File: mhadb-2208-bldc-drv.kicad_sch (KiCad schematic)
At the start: 46 parts, among them J1 TC2030, J2 Conn_01x04_Pin, J3 Conn_01x04, J4 Conn_01x04_Pin, SW1 SW_Push, SW4 SW_Push, U1 HT753-1, U2 SN65HVD230, U3 STM32F103C8Tx, Y1 8M

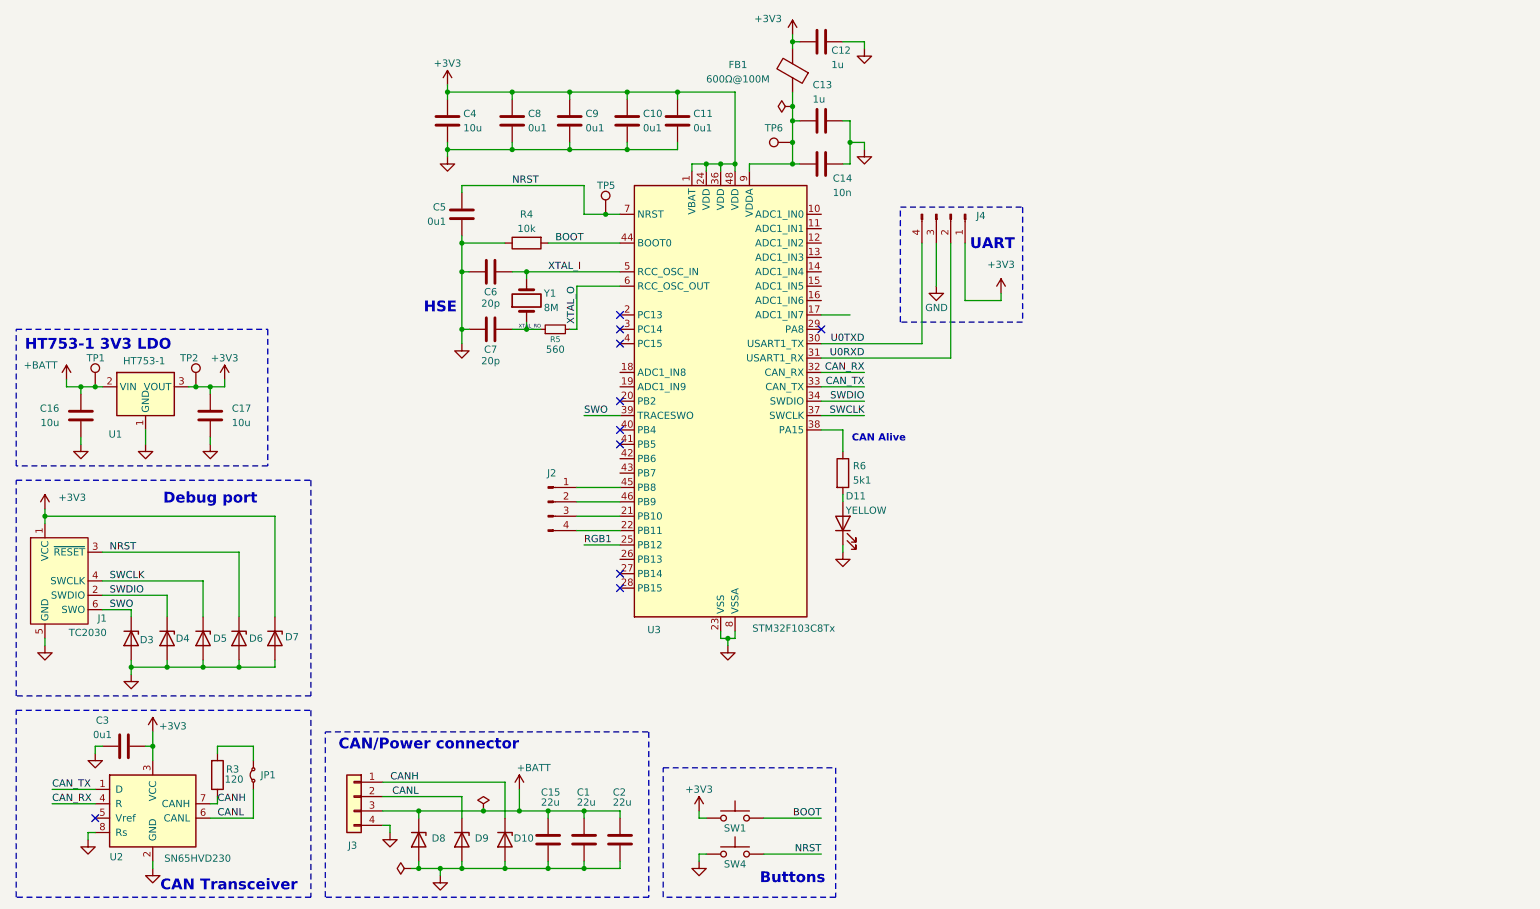
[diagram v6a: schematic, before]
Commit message: schem: add DRV8311 BLDC FOC driver
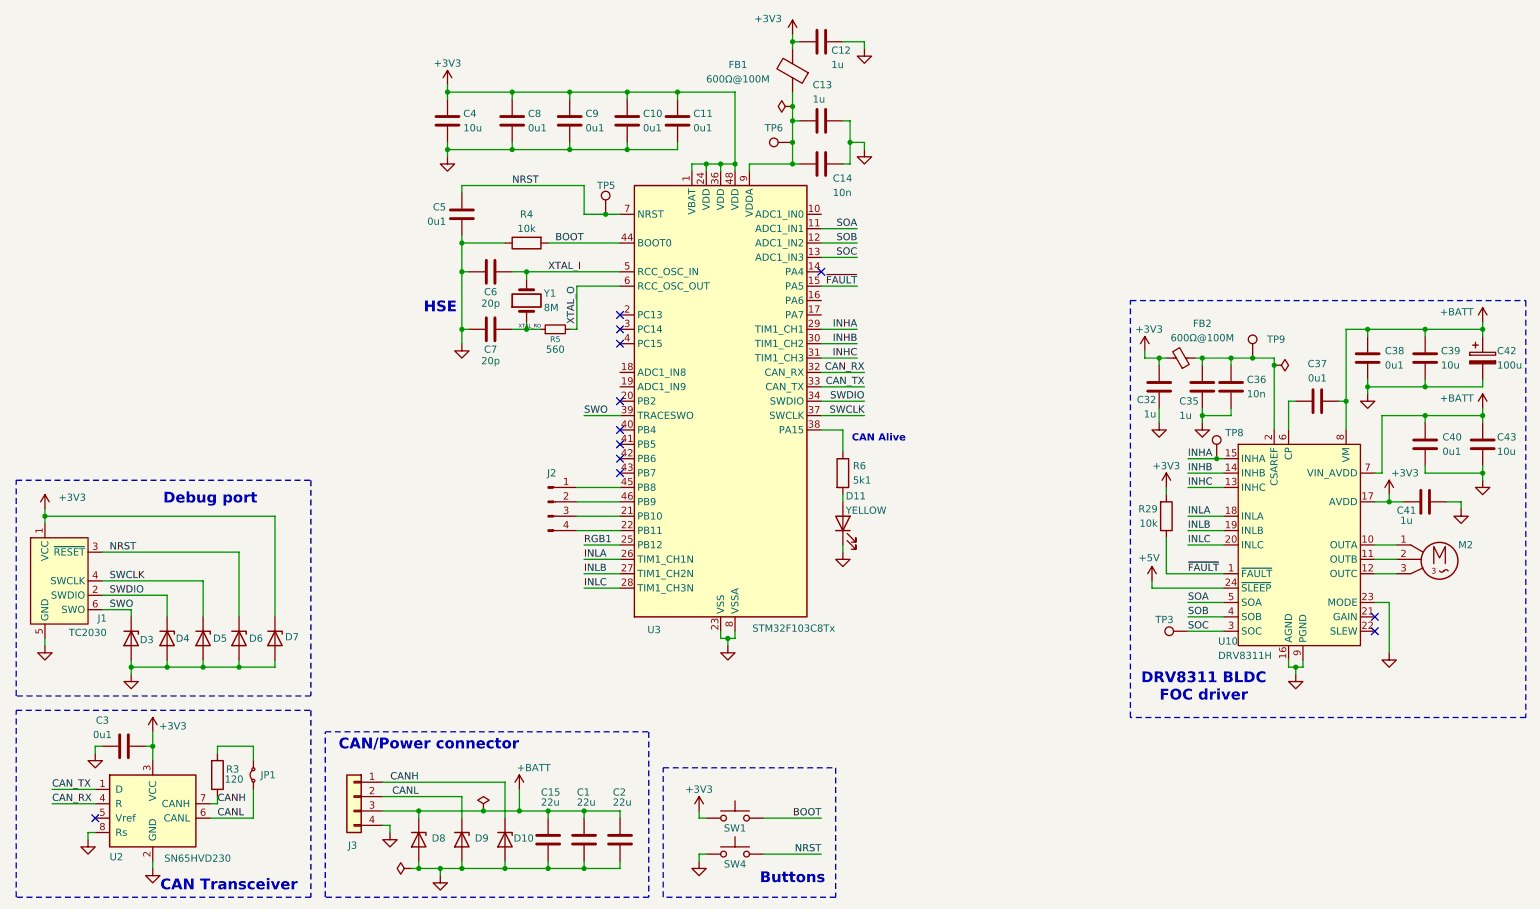
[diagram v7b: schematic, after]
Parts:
- removed C16, C17: 10u, Capacitor_SMD:C_0805_2012Metric, symbol Device:C
- removed J4: Conn_01x04_Pin, Connector_PinHeader_2.54mm:PinHeader_1x04_P2.54mm_Vertical, symbol Connector:Conn_01x04_Pin
- removed TP1, TP2: TestPoint, TestPoint:TestPoint_Pad_D2.0mm, symbol Connector:TestPoint
- removed U1: HT753-1, Package_TO_SOT_SMD:SOT-89-3, symbol Regulator_Linear:HT75xx-1-SOT89
- added C32, C35, C41: 1u, Capacitor_SMD:C_0402_1005Metric, symbol Device:C
- added C36: 10n, Capacitor_SMD:C_0402_1005Metric, symbol Device:C
- added C37, C38, C40: 0u1, Capacitor_SMD:C_0402_1005Metric, symbol Device:C
- added C39, C43: 10u, Capacitor_SMD:C_0805_2012Metric, symbol Device:C
- added C42: 100u, Capacitor_SMD:CP_Elec_6.3x7.7, symbol Device:C_Polarized
- added FB2: 600Ω@100M, Inductor_SMD:L_0805_2012Metric, symbol Device:FerriteBead_Small
- added M2: Motor_3_Phases, Connector_PinHeader_2.54mm:PinHeader_1x03_P2.54mm_Vertical, symbol GLCS:Motor_3_Phases
- added R29: 10k, Resistor_SMD:R_0402_1005Metric, symbol Device:R
- added TP3, TP8, TP9: TestPoint, TestPoint:TestPoint_Pad_D2.0mm, symbol Connector:TestPoint
- added U10: DRV8311H, GLCS:Texas_RRW0024A_WQFN-24-1EP_2x2mm_P0.4mmThermalVias, symbol GLCS:DRV8311H
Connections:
- net +3V3: now also C32.1, C41.1, FB2.2, R29.2, U10.17 (AVDD)
- net +BATT: now also C37.2, C38.2, C39.2, C40.2, C42.1, C43.2, U10.7 (VIN_AVDD), U10.8 (VM)
- net SOA: now reaches U3.11 (PA1)
- net SOA: now also U10.5 (SOA)
- net SOB: now reaches U3.12 (PA2)
- net SOB: now also U10.4 (SOB)
- net SOC: now reaches U3.13 (PA3)
- net SOC: now also TP3.1, U10.3 (SOC)
- net ~{FAULT}: now reaches U3.15 (PA5)
- net ~{FAULT}: now also R29.1, U10.1 (~{FAULT})
- net INLA: now reaches U3.26 (PB13)
- net INLA: now also U10.18 (INLA)
- net INLB: now reaches U3.27 (PB14)
- net INLB: now also U10.19 (INLB)
- net INLC: now reaches U3.28 (PB15)
- net INLC: now also U10.20 (INLC)
- net INHA: now reaches U3.29 (PA8)
- net INHA: now also TP8.1, U10.15 (INHA)
- net GND renamed EPAD
- net EPAD: now also C32.2, C35.2, C36.2, C38.1, C39.1, C40.1, C41.2, C42.2, C43.1, U10.16 (AGND), U10.23 (MODE), U10.25 (EPAD), U10.9 (PGND)
- net U0RXD renamed INHC
- net INHC: now also U10.13 (INHC)
- net U0TXD renamed INHB
- net INHB: now also U10.14 (INHB)
- new net: C35.1, C36.1, FB2.1, TP9.1, U10.2 (CSAREF)
- new net: M2.1, U10.10 (OUTA)
- new net: M2.2, U10.11 (OUTB)
- new net: M2.3, U10.12 (OUTC)
- new net: C37.1, U10.6 (CP)
- new net +5V: U10.24 (~{SLEEP})
- no-connect marks 10 -> 12
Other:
- note added: "DRV8311 BLDC FOC driver"
- note removed: "HT753-1 3V3 LDO"
- note removed: "UART"

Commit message: schem: add AS5600 magnetic encoder
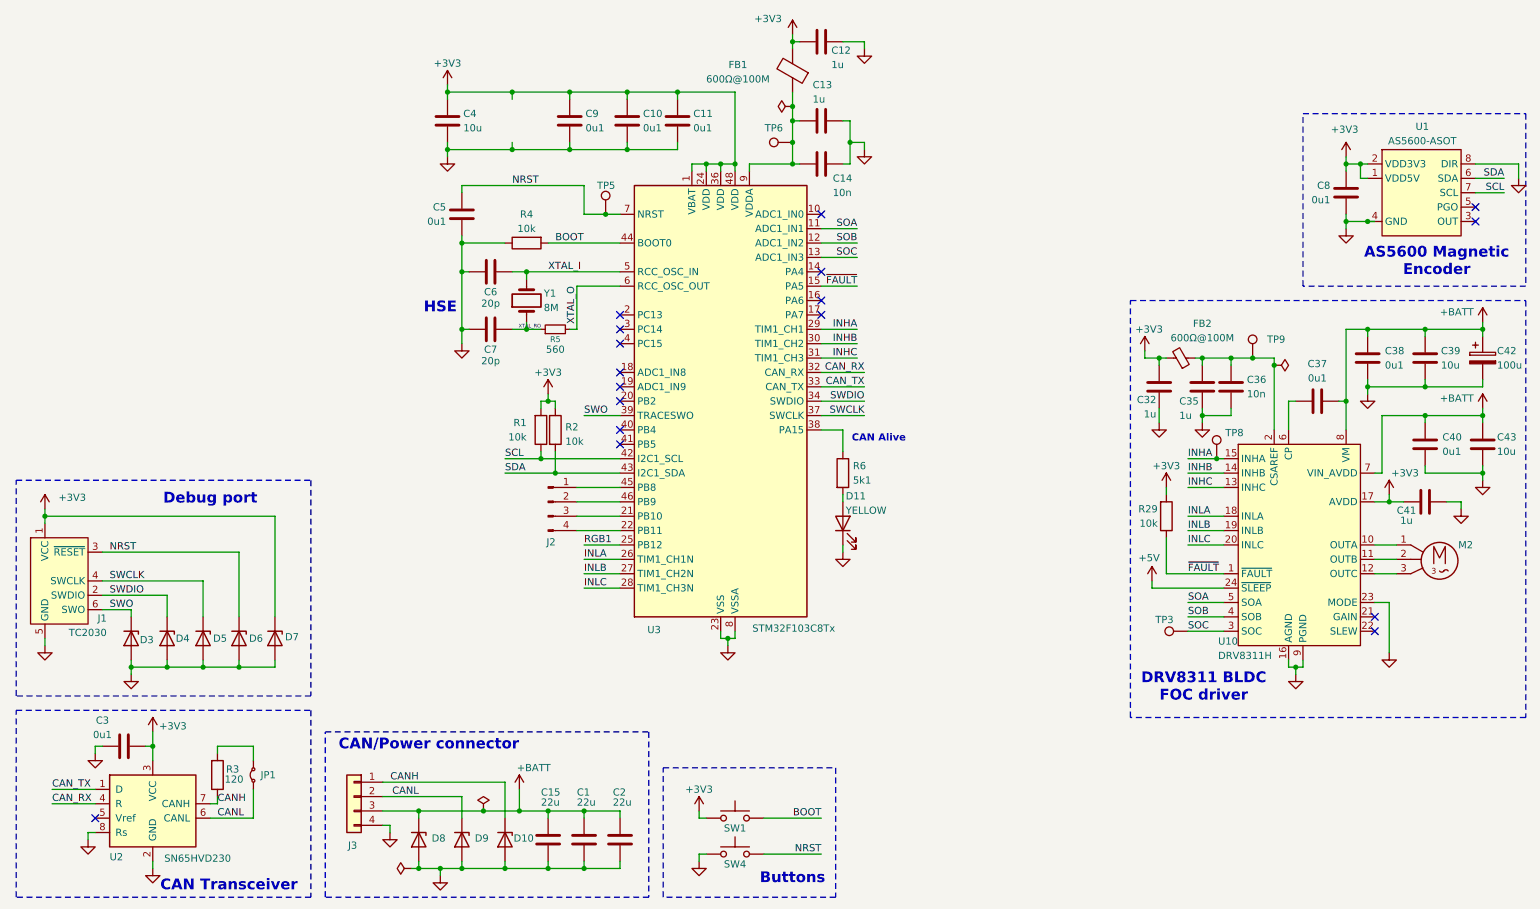
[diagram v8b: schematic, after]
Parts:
- added R1, R2: 10k, Resistor_SMD:R_0402_1005Metric, symbol Device:R
- added U1: AS5600-ASOT, Package_SO:SOIC-8_3.9x4.9mm_P1.27mm, symbol GLCS:AS5600
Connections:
- net +3V3: now also R1.2, R2.1, U1.1 (VDD5V), U1.2 (VDD3V3)
- net EPAD: now also U1.4 (GND), U1.8 (DIR)
- net SCL: now reaches U3.42 (PB6)
- net SCL: now also R1.1, U1.7 (SCL)
- net SDA: now reaches U3.43 (PB7)
- net SDA: now also R2.2, U1.6 (SDA)
- no-connect marks 12 -> 17
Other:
- note added: "AS5600 Magnetic Encoder"
- moved on the sheet: C8
